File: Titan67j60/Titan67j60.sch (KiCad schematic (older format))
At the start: 63 parts, among them J1 CONN_01X16, J18 CONN_01X02, J2 WiFi/GSM, J3 RJ45-TRANSFO, J30 CONN_01X05, U1 LTV-354T, U10 PC817, U11 TPS54308, U17 DRV8872, U2 ULN2003D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

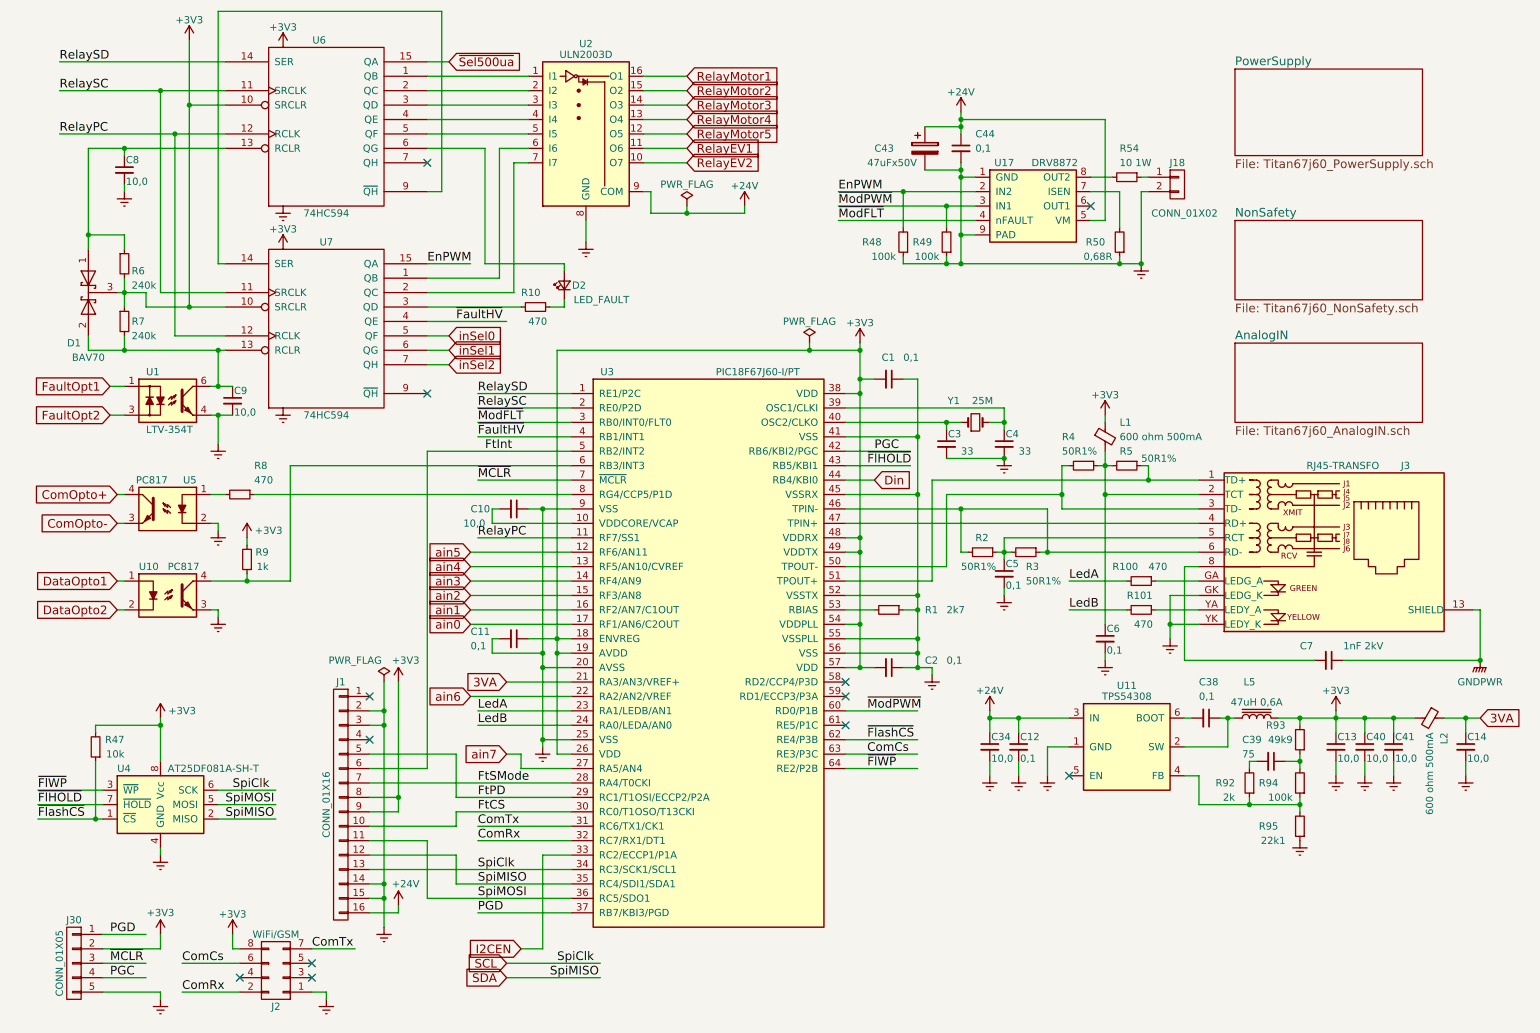
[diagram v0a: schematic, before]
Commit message: Microchip стек мигает светодиодом и получает IP адрес
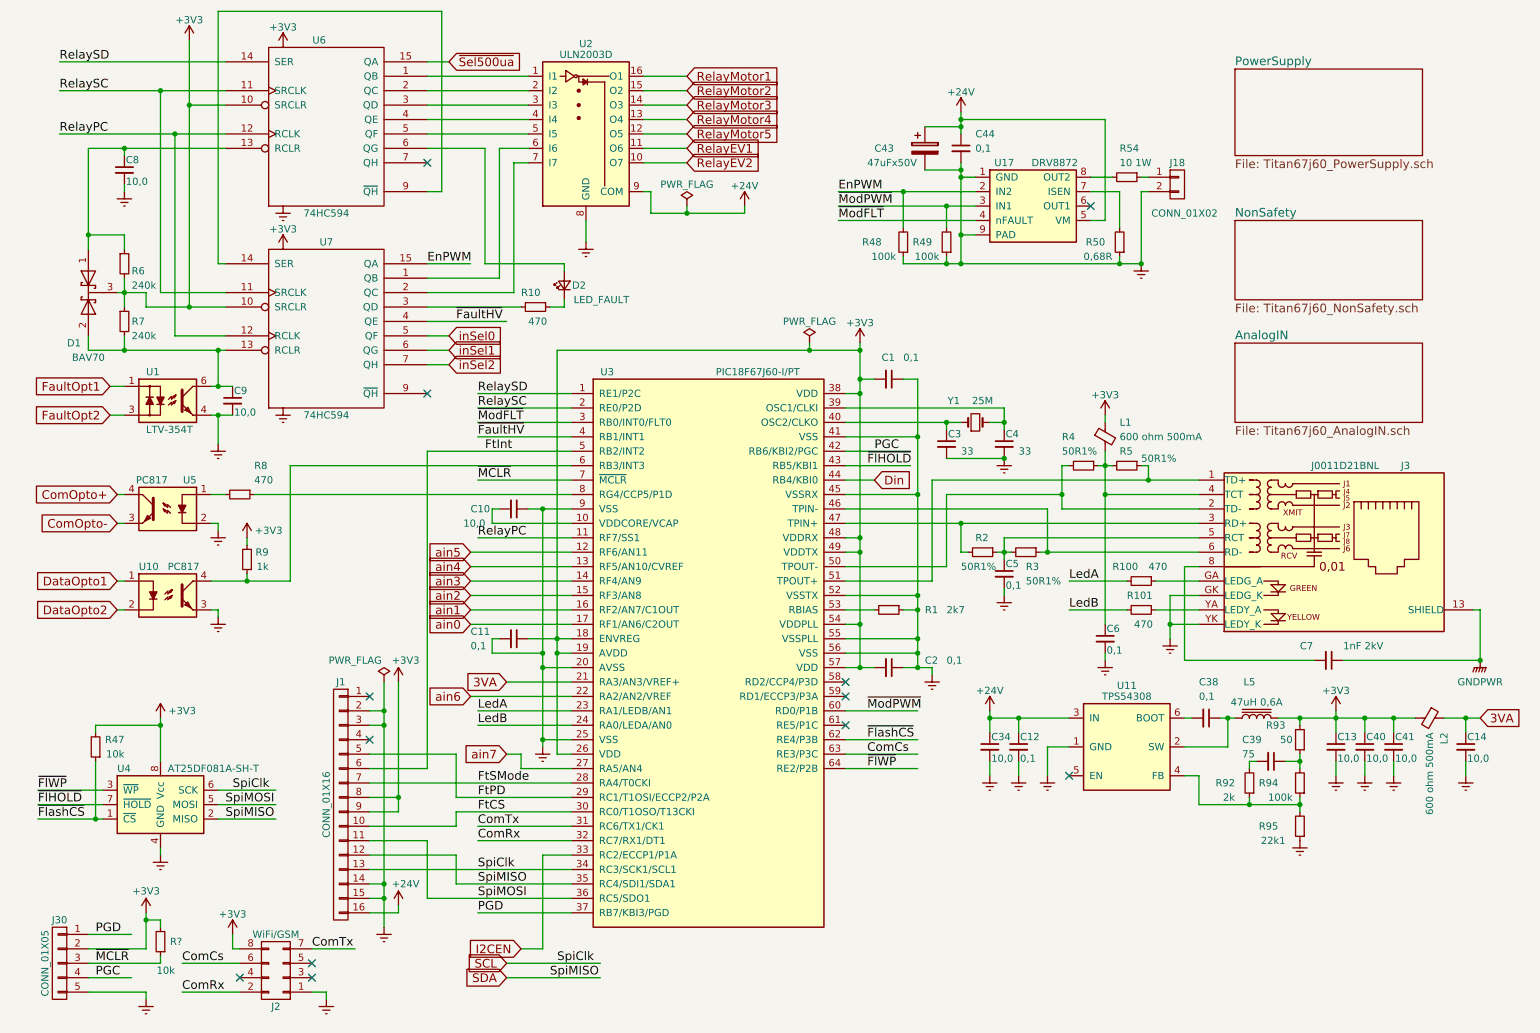
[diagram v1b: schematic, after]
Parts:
- removed J3: RJ45-TRANSFO, LehmanKiPatterns:RJ45_TRANS_J0011D21BNL, symbol RJ45-TRANSFO
- added J3: J0011D21BNL, symbol J0011D21BNL
- added R?: 10k, Resistors_SMD:R_0805, symbol R_Small
- R93: value 49k9 -> 50
- U1: footprint Housings_DIP:DIP-6_W7.62mm_SMD -> (none)
- U4: footprint Housings_SOIC:SOIC-8_3.9x4.9mm_Pitch1.27mm -> Housings_SOIC:SO-8_5.3x6.2mm_Pitch1.27mm
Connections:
- wire segments 307 -> 310
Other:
- moved on the sheet: J30
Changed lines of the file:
@@
-$EndComp
-$Comp
-L RJ45-TRANSFO J3
-U 1 1 595D3E6A
-P 10050 4350
-F 0 "J3" H 10150 4950 50  0000 L CNN
-F 1 "RJ45-TRANSFO" H 10000 4950 50  0000 R CNN
-F 2 "LehmanKiPatterns:RJ45_TRANS_J0011D21BNL" H 10050 4350 50  0001 C CNN
-F 3 "" H 10050 4350 50  0001 C CNN
-	1    10050 4350
-	1    0    0    -1
 $EndComp
 $Comp
@@
 F 0 "U1" H 1450 3500 50  0000 L CNN
 F 1 "LTV-354T" H 1450 3100 50  0000 L CNN
-F 2 "Housings_DIP:DIP-6_W7.62mm_SMD" H 1400 3100 50  0001 L CIN
+F 2 "" H 1400 3100 50  0001 L CIN
 F 3 "" H 1625 3300 50  0001 L CNN
 	1    1600 3300
@@
 F 0 "U4" H 1250 6350 50  0000 L CNN
 F 1 "AT25DF081A-SH-T" H 1600 6350 50  0000 L CNN
-F 2 "Housings_SOIC:SOIC-8_3.9x4.9mm_Pitch1.27mm" H 1200 6050 50  0001 C CNN
+F 2 "Housings_SOIC:SO-8_5.3x6.2mm_Pitch1.27mm" H 1200 6050 50  0001 C CNN
 F 3 "" H 1200 6050 50  0001 C CNN
 	1    1550 6100
@@
 L CONN_01X05 J30
 U 1 1 59A99668
-P 950 7200
-F 0 "J30" H 950 7500 50  0000 C CNN
-F 1 "CONN_01X05" V 1050 7200 50  0000 C CNN
-F 2 "Connectors_Terminal_Blocks:TerminalBlock_Pheonix_MPT-2.54mm_5pol" H 950 7200 50  0001 C CNN
-F 3 "" H 950 7200 50  0001 C CNN
-	1    950  7200
+P 850 7200
+F 0 "J30" H 850 7500 50  0000 C CNN
+F 1 "CONN_01X05" V 950 7200 50  0000 C CNN
+F 2 "Connectors_Terminal_Blocks:TerminalBlock_Pheonix_MPT-2.54mm_5pol" H 850 7200 50  0001 C CNN
+F 3 "" H 850 7200 50  0001 C CNN
+	1    850  7200
 	-1   0    0    -1
 $EndComp
@@
 L Earth #PWR035
 U 1 1 59A99B7B
-P 1550 7450
-F 0 "#PWR035" H 1550 7200 50  0001 C CNN
-F 1 "Earth" H 1550 7300 50  0001 C CNN
-F 2 "" H 1550 7450 50  0001 C CNN
-F 3 "" H 1550 7450 50  0001 C CNN
-	1    1550 7450
+P 1450 7450
+F 0 "#PWR035" H 1450 7200 50  0001 C CNN
+F 1 "Earth" H 1450 7300 50  0001 C CNN
+F 2 "" H 1450 7450 50  0001 C CNN
+F 3 "" H 1450 7450 50  0001 C CNN
+	1    1450 7450
 	1    0    0    -1
 $EndComp
@@
 L +3V3 #PWR036
 U 1 1 59A99C3A
-P 1550 7000
-F 0 "#PWR036" H 1550 6850 50  0001 C CNN
-F 1 "+3V3" H 1550 7150 50  0000 C CNN
-F 2 "" H 1550 7000 50  0001 C CNN
-F 3 "" H 1550 7000 50  0001 C CNN
-	1    1550 7000
+P 1450 6850
+F 0 "#PWR036" H 1450 6700 50  0001 C CNN
+F 1 "+3V3" H 1450 7000 50  0000 C CNN
+F 2 "" H 1450 6850 50  0001 C CNN
+F 3 "" H 1450 6850 50  0001 C CNN
+	1    1450 6850
 	1    0    0    -1
 $EndComp
 Text Label 3750 3850 0    60   ~ 0
 ~MCLR
-Text Label 1200 7200 0    60   ~ 0
+Text Label 1100 7200 0    60   ~ 0
 ~MCLR
 $Comp
@@
 P 9450 5650
 F 0 "R93" H 9550 5550 50  0000 L CNN
-F 1 "49k9" H 9500 5650 50  0000 L CNN
+F 1 "50" H 9500 5650 50  0000 L CNN
 F 2 "Resistors_SMD:R_0603" H 9450 5650 50  0001 C CNN
 F 3 "" H 9450 5650 50  0001 C CNN
@@
 	0    1    1    0
 $EndComp
-Text Label 1200 7300 0    60   ~ 0
+Text Label 1100 7300 0    60   ~ 0
 PGC
-Text Label 1200 7000 0    60   ~ 0
+Text Label 1100 7000 0    60   ~ 0
 PGD
 Text Label 3750 6850 0    60   ~ 0
@@
 Wire Wire Line
 	7150 4350 7100 4350
-Wire Wire Line
-	7100 4350 7100 4050
-Connection ~ 7100 4050
 Wire Wire Line
 	8750 4250 7400 4250
@@
 	3400 2350 3700 2350
 Wire Wire Line
-	1150 7400 1550 7400
-Wire Wire Line
-	1550 7400 1550 7450
-Wire Wire Line
-	1150 7100 1550 7100
-Wire Wire Line
-	1550 7100 1550 7000
-Wire Wire Line
-	1150 7200 1450 7200
+	1050 7400 1450 7400
+Wire Wire Line
+	1450 7400 1450 7450
+Wire Wire Line
+	1050 7100 1450 7100
+Wire Wire Line
+	1450 7100 1450 6850
+Wire Wire Line
+	1050 7200 1550 7200
 Wire Wire Line
 	4400 3850 3750 3850
@@
 	4900 1650 5200 1650
 Wire Wire Line
-	1150 7000 1450 7000
-Wire Wire Line
-	1150 7300 1450 7300
+	1050 7000 1350 7000
+Wire Wire Line
+	1050 7300 1350 7300
 Wire Wire Line
 	4400 6850 3750 6850
@@
 	7200 2150 7100 2150
 Connection ~ 7100 2150
+$Comp
+L R_Small R?
+U 1 1 5A12E61F
+P 1550 7050
+F 0 "R?" H 1400 7050 50  0000 L CNN
+F 1 "10k" H 1450 7250 50  0000 L CNN
+F 2 "Resistors_SMD:R_0805" H 1550 7050 50  0001 C CNN
+F 3 "" H 1550 7050 50  0001 C CNN
+	1    1550 7050
+	-1   0    0    1
+$EndComp
+Wire Wire Line
+	1550 7200 1550 7150
+Wire Wire Line
+	1550 6950 1550 6900
+Wire Wire Line
+	1550 6900 1450 6900
+Connection ~ 1450 6900
+$Comp
+L J0011D21BNL J3
+U 1 1 5A1EB7E9
+P 10050 4350
+F 0 "J3" H 10150 4950 50  0000 L CNN
+F 1 "J0011D21BNL" H 10000 4950 50  0000 R CNN
+F 2 "" H 10050 4350 50  0001 C CNN
+F 3 "" H 10050 4350 50  0001 C CNN
+	1    10050 4350
+	1    0    0    -1
+$EndComp
+Wire Wire Line
+	7100 4350 7100 4150
+Connection ~ 7100 4150
 $EndSCHEMATC

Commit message: Работает минимальный набор до прикручивания TCP IP
Signed-off-by: Lehman3065 <lehman3065@gmail.com>
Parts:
- added C?: 0,1, Capacitors_SMD:C_0603, symbol C_Small
- added R?: 220, Resistors_SMD:R_0805, symbol R_Small
- C8, C9: value 10,0 -> 1,0
- U17: value DRV8872 -> DRV8872 8816!!!
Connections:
- net labels added: Data
- wire segments 310 -> 318
- no-connect marks 12 -> 10
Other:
- moved on the sheet: C9, J2, J30, R47, R8, R9, R?, U1, U10, U4, U5
